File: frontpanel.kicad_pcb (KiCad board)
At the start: 2 copper layers, 172.5 x 128.3 mm, 104 parts, among them J601 PJ301CM, J602 PJ301CM, J603 PJ301BM, J604 PJ301BM, J605 PJ301BM, J606 PJ301BM, J607 PJ301BM, J608 PJ301BM, J609 PJ301BM, J610 PJ301BM, J611 PJ301BM, J612 PJ301BM, J613 PJ301BM, J614 PJ301BM, J615 PJ301BM, J616 PJ301BM, J617 PJ301BM, J618 PJ301BM, J619 PJ301BM, J620 PJ301BM, J621 PJ301BM, J622 PJ301BM, J623 PJ301BM, J624 PJ301BM, J625 PJ301BM, J626 PJ301BM, SW301 TL1105T, SW302 TL1105T, SW303 TL1105T, SW304 TL1105T, SW305 TL1105T, SW317 TL1105T, SW318 TL1105T, SW319 TL1105T, SW320 TL1105T, SW321 TL1105T, SW322 TL1105T, SW323 TL1105T, SW324 TL1105T, SW325 TL1105T, SW326 TL1105T, SW327 TL1105T, SW328 TL1105T, SW329 TL1105T, SW330 TL1105T, SW331 TL1105T, SW332 TL1105T, SW333 TL1105T, SW334 TL1105T, SW335 TL1105T, SW336 TL1105T, SW337 TL1105T, SW338 TL1105T, SW339 TL1105T, SW340 TL1105T

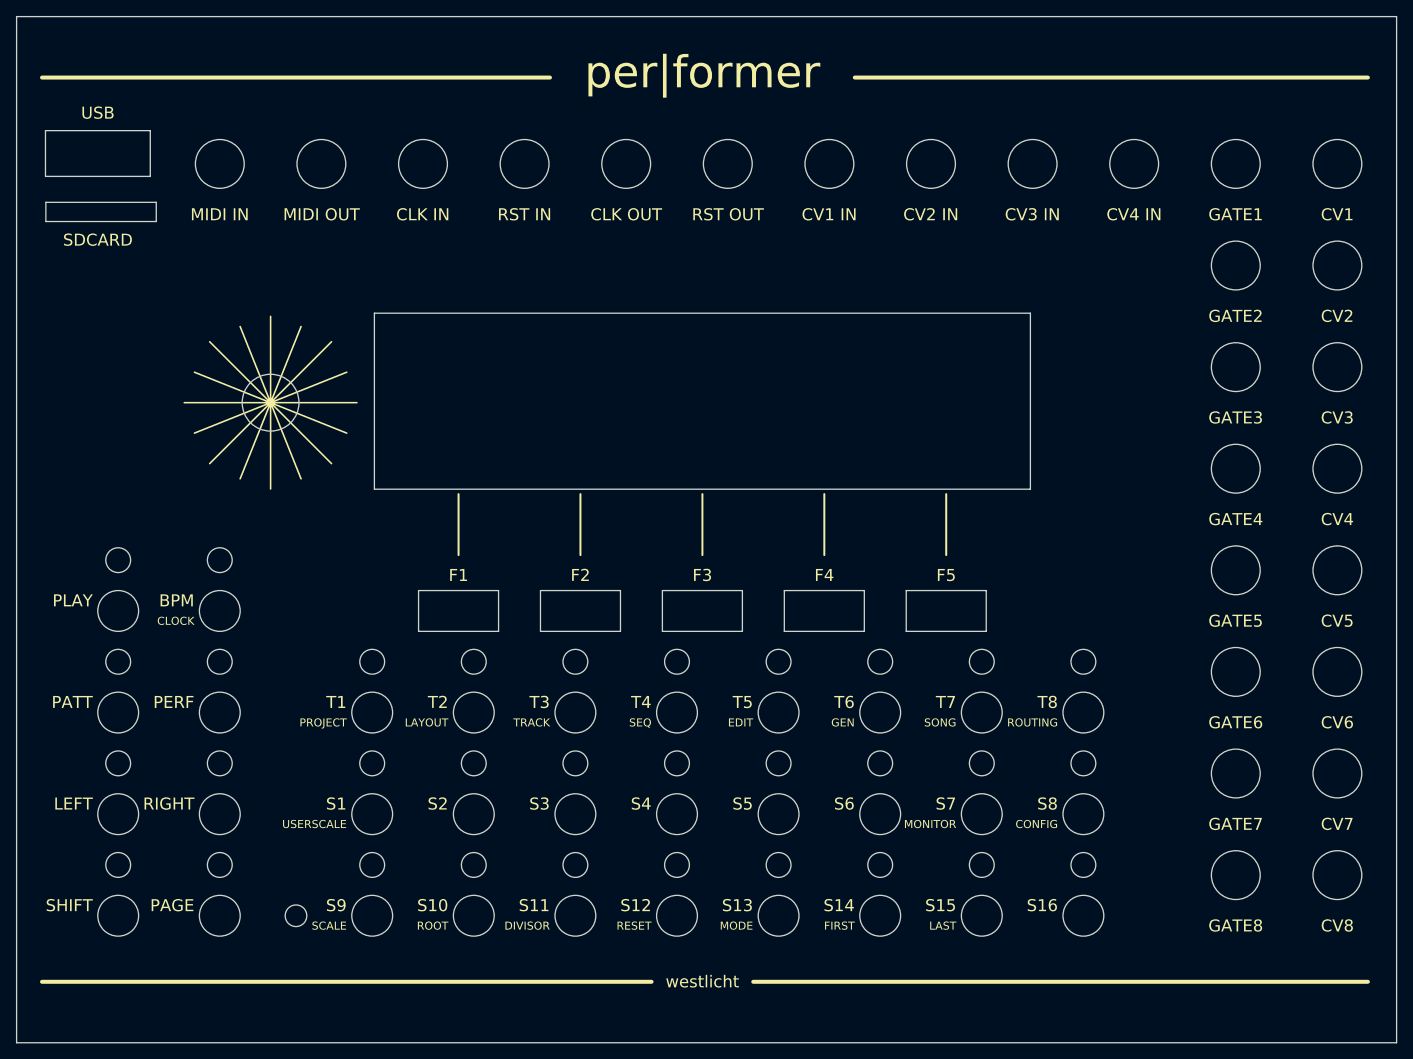
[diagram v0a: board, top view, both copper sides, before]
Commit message: updated frontpanel
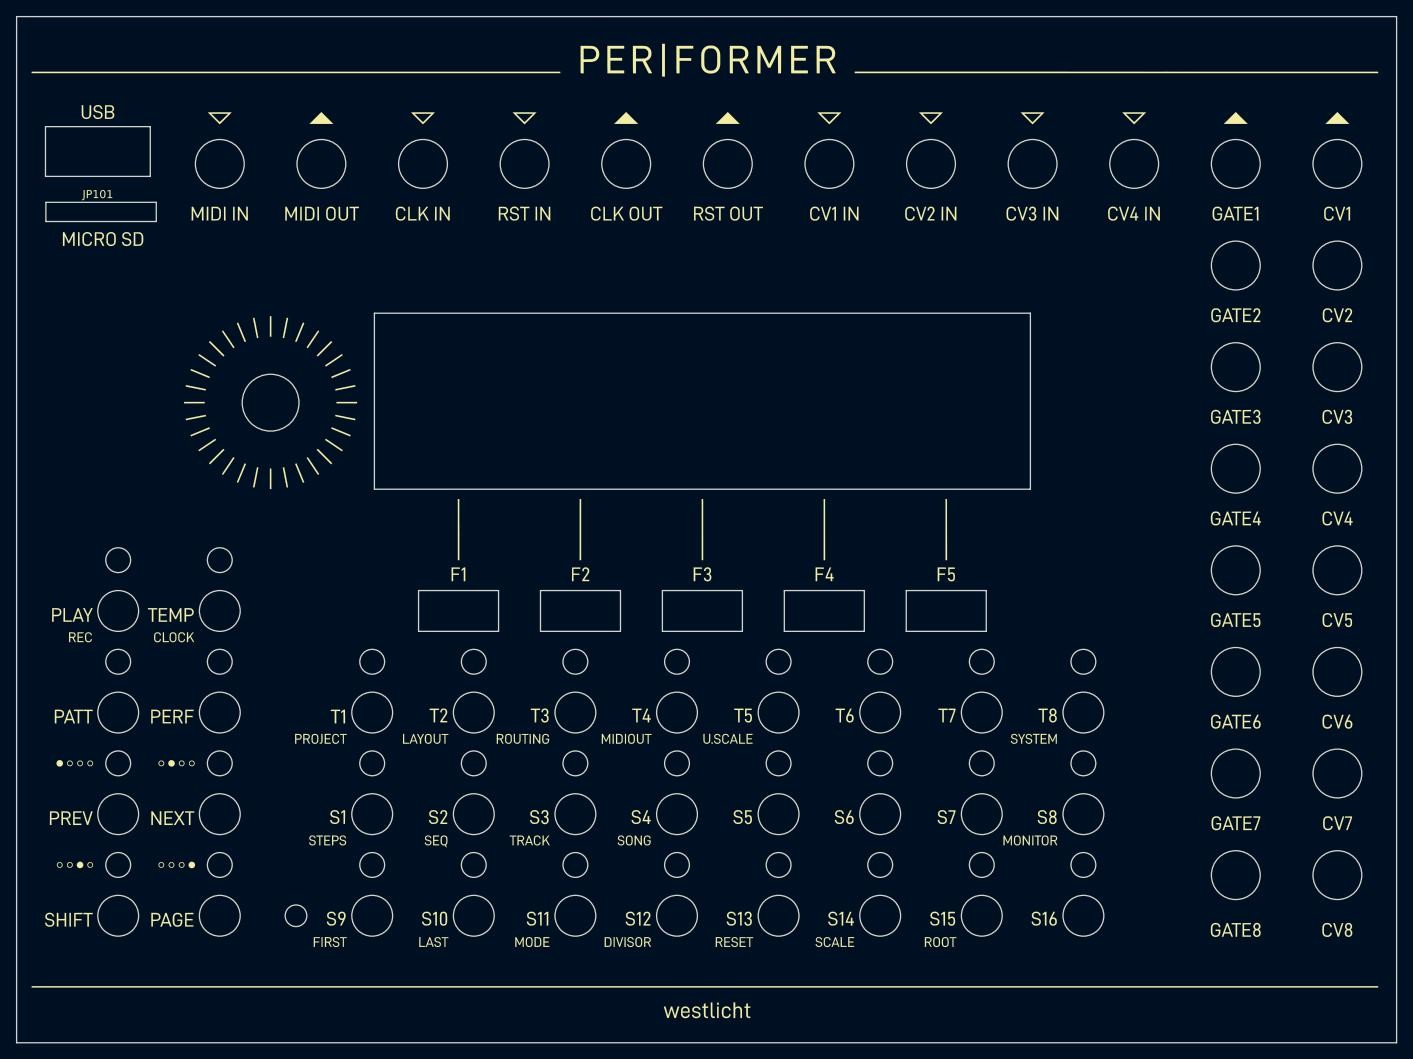
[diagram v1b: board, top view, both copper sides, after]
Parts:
- added G***: LOGO, frontpanel:frontpanel, F.Cu at (162.4, 91.4)
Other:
- board text removed: "+12V"
- board text removed: "-12V"
- board text removed: "BOOT"
- board text removed: "BPM"
- board text removed: "CLK IN"
- board text removed: "CLK OUT"
- board text removed: "CLOCK"
- board text removed: "CONFIG"
- board text removed: "CV1"
- board text removed: "CV1 IN"
- board text removed: "CV2"
- board text removed: "CV2 IN"
- board text removed: "CV3"
- board text removed: "CV3 IN"
- board text removed: "CV4"
- board text removed: "CV4 IN"
- board text removed: "CV5"
- board text removed: "CV6"
- board text removed: "CV7"
- board text removed: "CV8"
- board text removed: "DIVISOR"
- board text removed: "EDIT"
- board text removed: "F1"
- board text removed: "F2"
- board text removed: "F3"
- board text removed: "F4"
- board text removed: "F5"
- board text removed: "FIRST"
- board text removed: "GATE1"
- board text removed: "GATE2"
- board text removed: "GATE3"
- board text removed: "GATE4"
- board text removed: "GATE5"
- board text removed: "GATE6"
- board text removed: "GATE7"
- board text removed: "GATE8"
- board text removed: "GEN"
- board text removed: "GND"
- board text removed: "JTAG"
- board text removed: "LAST"
- board text removed: "LAYOUT"
- board text removed: "LEFT"
- board text removed: "MIDI IN"
- board text removed: "MIDI OUT"
- board text removed: "MODE"
- board text removed: "MONITOR"
- board text removed: "PAGE"
- board text removed: "PATT"
- board text removed: "PERF"
- board text removed: "PLAY"
- board text removed: "PROJECT"
- board text removed: "RED LINE"
- board text removed: "RESET"
- board text removed: "RIGHT"
- board text removed: "ROOT"
- board text removed: "ROUTING"
- board text removed: "RST IN"
- board text removed: "RST OUT"
- board text removed: "RX"
- board text removed: "S1"
- board text removed: "S10"
- board text removed: "S11"
- board text removed: "S12"
- board text removed: "S13"
- board text removed: "S14"
- board text removed: "S15"
- board text removed: "S16"
- board text removed: "S2"
- board text removed: "S3"
- board text removed: "S4"
- board text removed: "S5"
- board text removed: "S6"
- board text removed: "S7"
- board text removed: "S8"
- board text removed: "S9"
- board text removed: "SCALE"
- board text removed: "SDCARD"
- board text removed: "SEQ"
- board text removed: "SERIAL"
- board text removed: "SHIFT"
- board text removed: "SONG"
- board text removed: "T1"
- board text removed: "T2"
- board text removed: "T3"
- board text removed: "T4"
- board text removed: "T5"
- board text removed: "T6"
- board text removed: "T7"
- board text removed: "T8"
- board text removed: "TRACK"
- board text removed: "TX"
- board text removed: "USB"
- board text removed: "USERSCALE"
- board text removed: "cc-by-sa Simon Kallweit 2018 board revision 0.2"
- board text removed: "per|former"
- board text removed: "westlicht"
